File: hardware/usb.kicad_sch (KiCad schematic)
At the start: 51 parts, among them J1 USB_C_Receptacle_USB2.0_14P, J27 USB_C_Receptacle_USB2.0_14P, J28 USB_C_Receptacle_USB2.0_14P, Q1 BSC098N10NS5, Q2 BSC098N10NS5, SW1 SW_DIP_x03, SW2 SW_DIP_x03, U2 CH224K, U20 LM5050-1, U21 LM5050-1, U22 CH224K

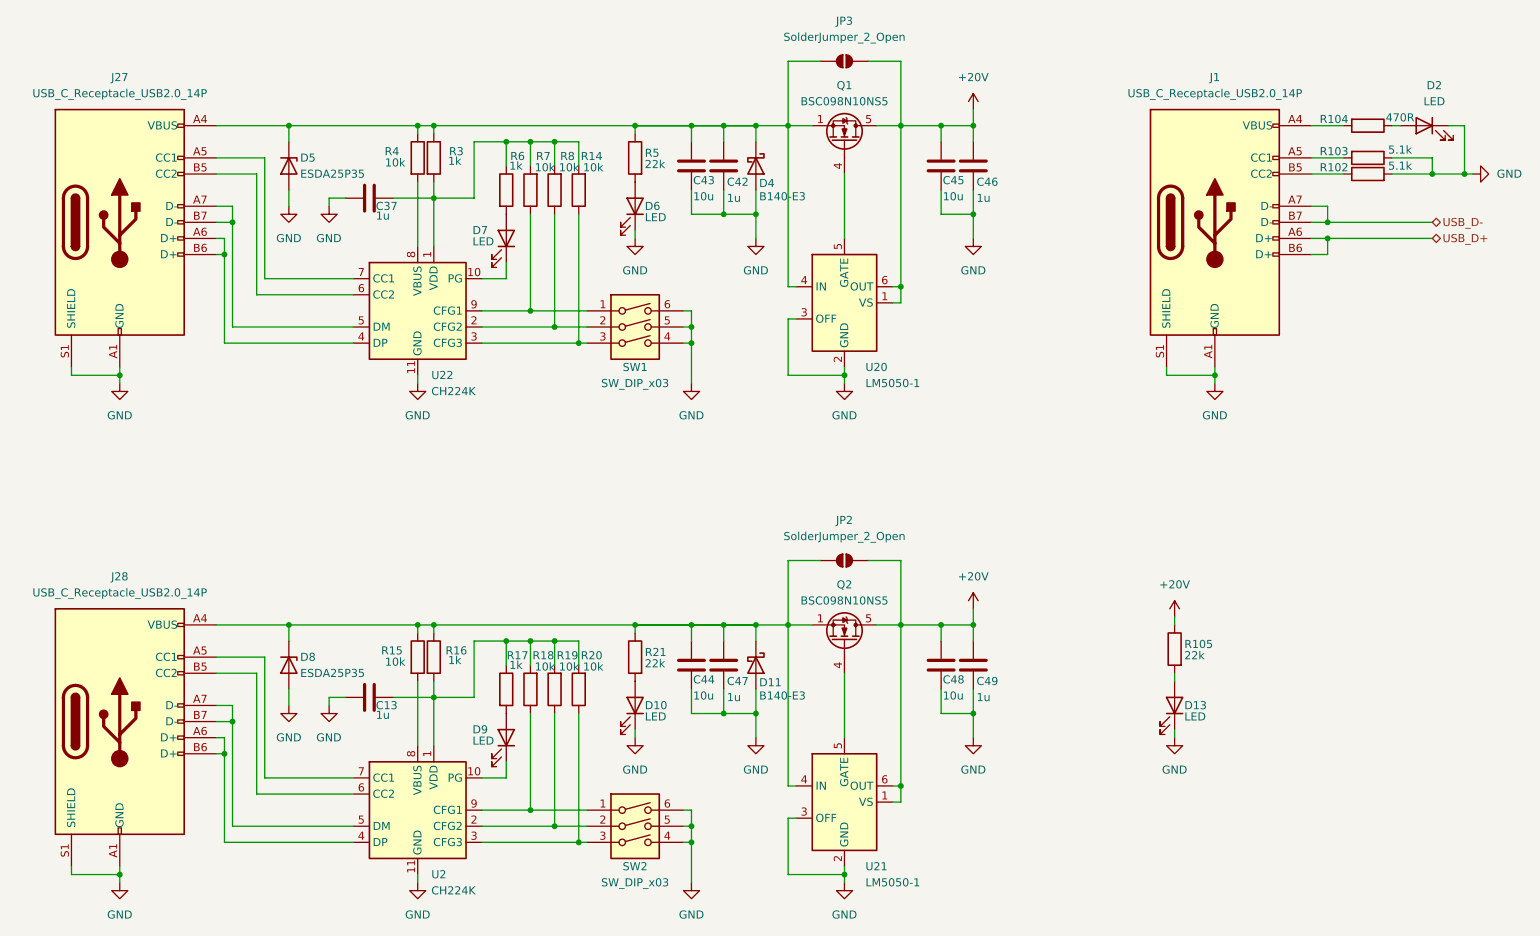
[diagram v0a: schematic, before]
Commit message: complete schematic wiring
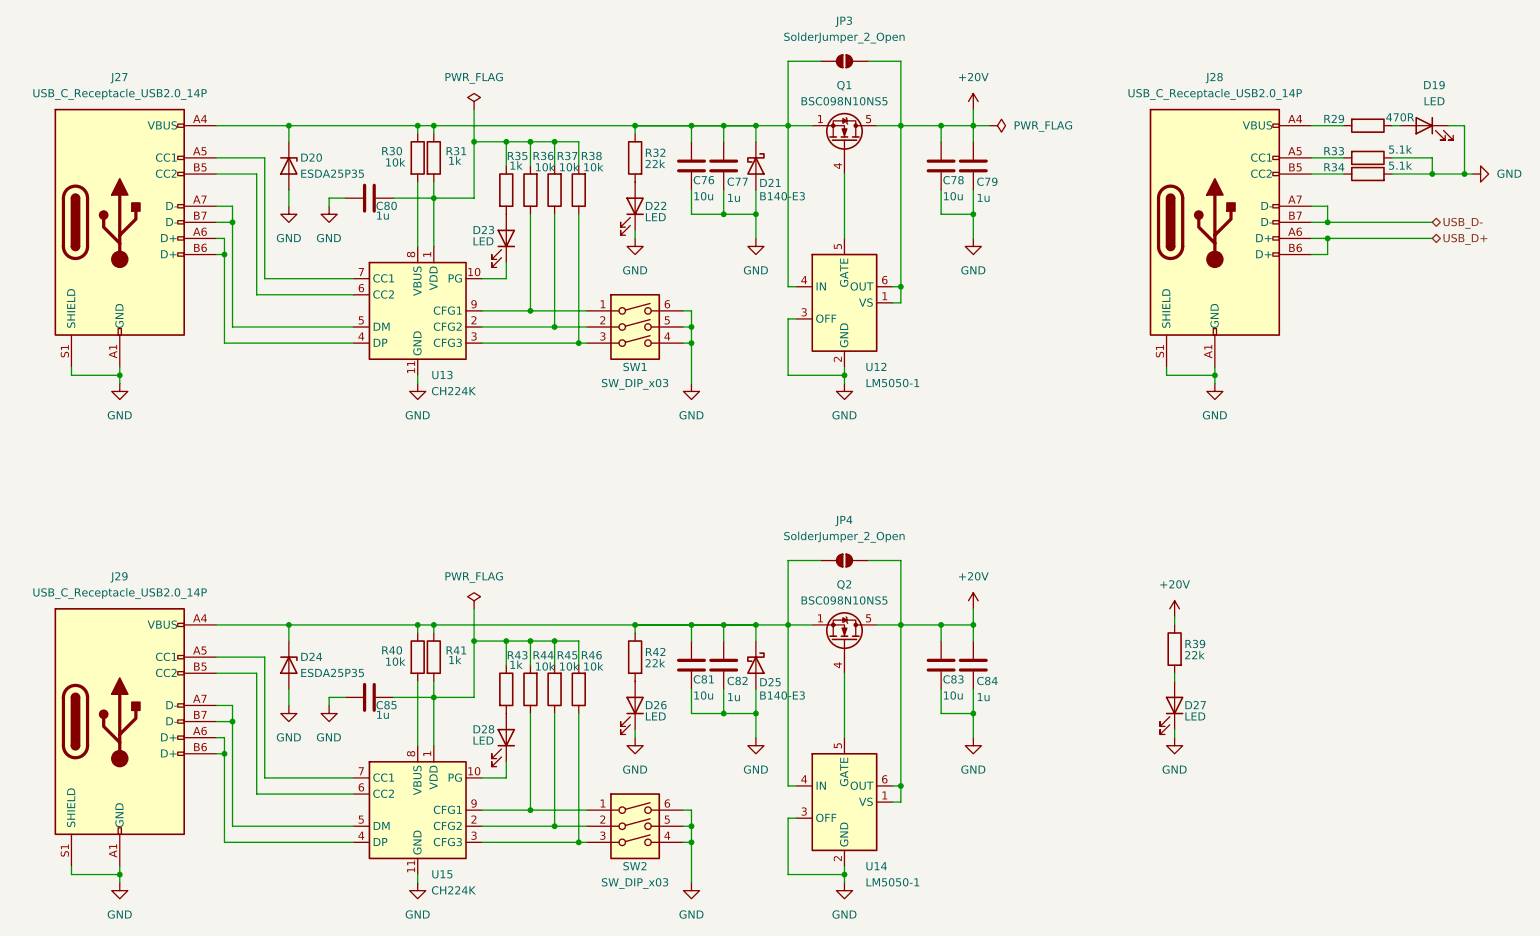
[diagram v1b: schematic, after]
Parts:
- renumbered C43 to C76, C42 to C77, C45 to C78, C46 to C79, C37 to C80, C44 to C81, C47 to C82, C48 to C83, C49 to C84, C13 to C85, D2 to D19, D5 to D20, D4 to D21, D6 to D22, D7 to D23, D8 to D24, D11 to D25, D10 to D26, D13 to D27, D9 to D28, J1 to J28, J28 to J29, JP2 to JP4, R104 to R29, R4 to R30, R3 to R31, R5 to R32, R103 to R33, R102 to R34, R6 to R35, R7 to R36, R8 to R37, R14 to R38, R105 to R39, R15 to R40, R16 to R41, R21 to R42, R17 to R43, R18 to R44, R19 to R45, R20 to R46, U20 to U12, U22 to U13, U21 to U14, U2 to U15

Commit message: update power system + add LCSC part numbers
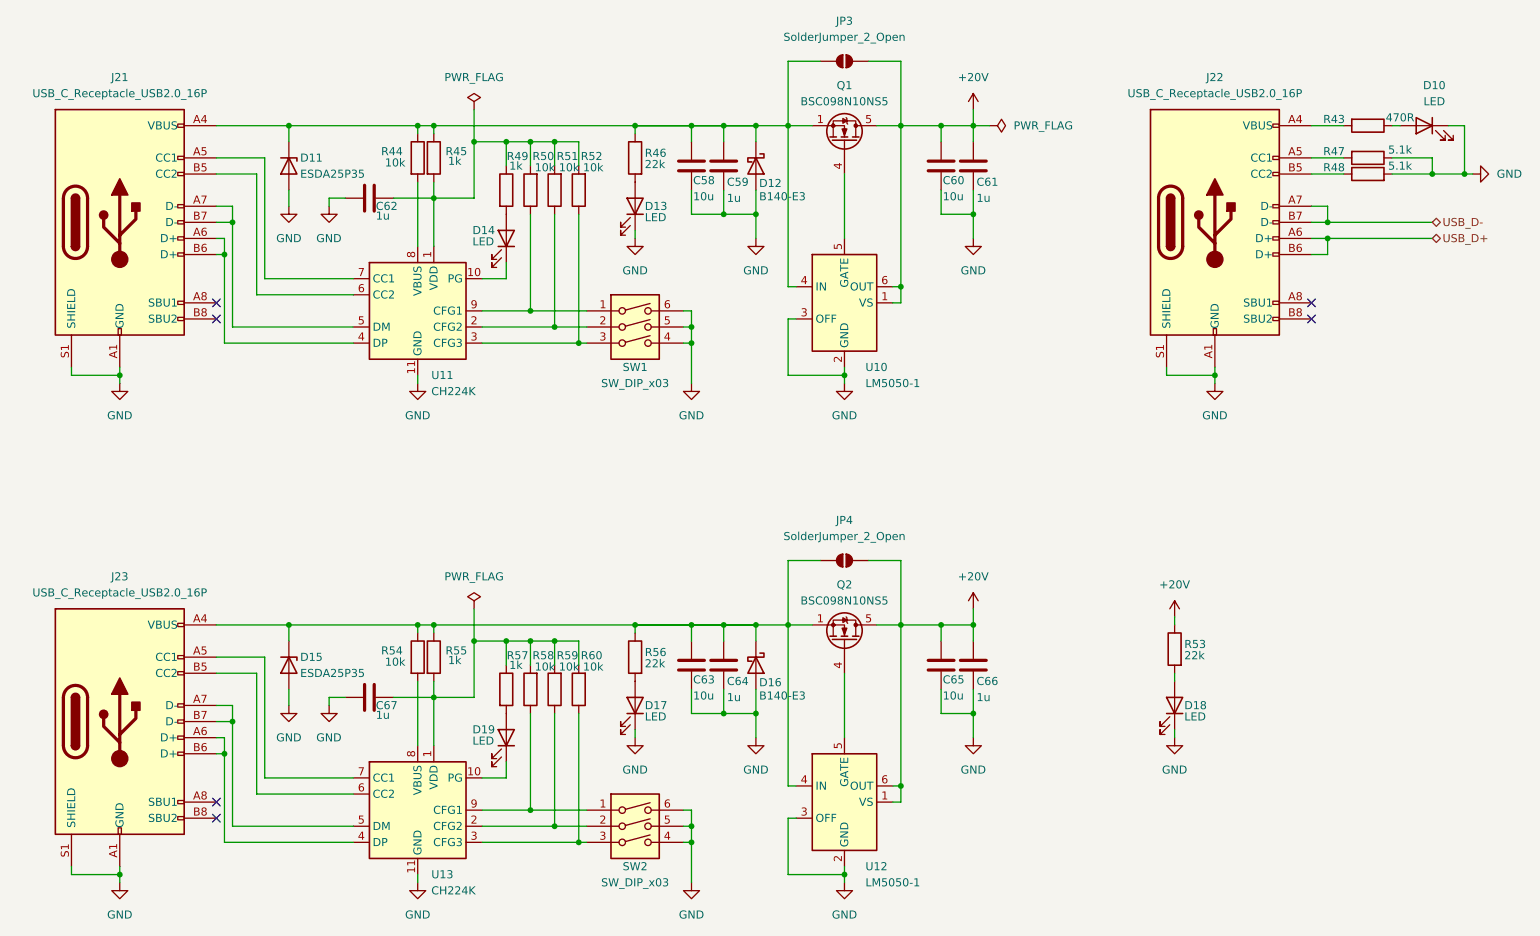
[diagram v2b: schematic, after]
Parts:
- removed J27, J28, J29: USB_C_Receptacle_USB2.0_14P, symbol Connector:USB_C_Receptacle_USB2.0_14P
- added J21, J22, J23: USB_C_Receptacle_USB2.0_16P, Connector_USB:USB_C_Receptacle_GCT_USB4105-xx-A_16P_TopMnt_Horizontal, symbol Connector:USB_C_Receptacle_USB2.0_16P
- C58: renamed from C76; footprint (none) -> Capacitor_SMD:C_1206_3216Metric; LCSC (none) -> C13585
- C59: renamed from C77; footprint (none) -> Capacitor_SMD:C_0805_2012Metric; LCSC (none) -> C28323
- C60: renamed from C78; footprint (none) -> Capacitor_SMD:C_1206_3216Metric; LCSC (none) -> C13585
- C61: renamed from C79; footprint (none) -> Capacitor_SMD:C_0805_2012Metric; LCSC (none) -> C28323
- C62: renamed from C80; footprint (none) -> Capacitor_SMD:C_0805_2012Metric; LCSC (none) -> C28323
- C63: renamed from C81; footprint (none) -> Capacitor_SMD:C_1206_3216Metric; LCSC (none) -> C13585
- C64: renamed from C82; footprint (none) -> Capacitor_SMD:C_0805_2012Metric; LCSC (none) -> C28323
- C65: renamed from C83; footprint (none) -> Capacitor_SMD:C_1206_3216Metric; LCSC (none) -> C13585
- C66: renamed from C84; footprint (none) -> Capacitor_SMD:C_0805_2012Metric; LCSC (none) -> C28323
- C67: renamed from C85; footprint (none) -> Capacitor_SMD:C_0805_2012Metric; LCSC (none) -> C28323
- D10: renamed from D19; footprint (none) -> LED_SMD:LED_0805_2012Metric; LCSC (none) -> C2297
- D11: renamed from D20; footprint (none) -> digital:D_1610_4027Metric; LCSC (none) -> C1974707
- D12: renamed from D21; LCSC (none) -> C2981056
- D13: renamed from D22; footprint (none) -> LED_SMD:LED_0805_2012Metric; LCSC (none) -> C2297
- D14: renamed from D23; footprint (none) -> LED_SMD:LED_0805_2012Metric; LCSC (none) -> C2297
- D15: renamed from D24; footprint (none) -> digital:D_1610_4027Metric; LCSC (none) -> C1974707
- D16: renamed from D25; LCSC (none) -> C2981056
- D17: renamed from D26; footprint (none) -> LED_SMD:LED_0805_2012Metric; LCSC (none) -> C2297
- D18: renamed from D27; footprint (none) -> LED_SMD:LED_0805_2012Metric; LCSC (none) -> C2297
- D19: renamed from D28; footprint (none) -> LED_SMD:LED_0805_2012Metric; LCSC (none) -> C2297
- JP3, JP4: footprint (none) -> Jumper:SolderJumper-2_P1.3mm_Open_RoundedPad1.0x1.5mm
- Q1, Q2: LCSC (none) -> C534398
- R43: renamed from R29; footprint (none) -> Resistor_SMD:R_0402_1005Metric; LCSC (none) -> C25117
- R44: renamed from R30; footprint (none) -> Resistor_SMD:R_0402_1005Metric; LCSC (none) -> C25744
- R45: renamed from R31; footprint (none) -> Resistor_SMD:R_0402_1005Metric; LCSC (none) -> C11702
- R46: renamed from R32; footprint (none) -> Resistor_SMD:R_0402_1005Metric; LCSC (none) -> C25768
- R47: renamed from R33; footprint (none) -> Resistor_SMD:R_0402_1005Metric; LCSC (none) -> C25905
- R48: renamed from R34; footprint (none) -> Resistor_SMD:R_0402_1005Metric; LCSC (none) -> C25905
- R49: renamed from R35; footprint (none) -> Resistor_SMD:R_0402_1005Metric; LCSC (none) -> C11702
- R50: renamed from R36; footprint (none) -> Resistor_SMD:R_0402_1005Metric; LCSC (none) -> C25744
- R51: renamed from R37; footprint (none) -> Resistor_SMD:R_0402_1005Metric; LCSC (none) -> C25744
- R52: renamed from R38; footprint (none) -> Resistor_SMD:R_0402_1005Metric; LCSC (none) -> C25744
- R53: renamed from R39; footprint (none) -> Resistor_SMD:R_0402_1005Metric; LCSC (none) -> C25768
- R54: renamed from R40; footprint (none) -> Resistor_SMD:R_0402_1005Metric; LCSC (none) -> C25744
- R55: renamed from R41; footprint (none) -> Resistor_SMD:R_0402_1005Metric; LCSC (none) -> C11702
- R56: renamed from R42; footprint (none) -> Resistor_SMD:R_0402_1005Metric; LCSC (none) -> C25768
- R57: renamed from R43; footprint (none) -> Resistor_SMD:R_0402_1005Metric; LCSC (none) -> C11702
- R58: renamed from R44; footprint (none) -> Resistor_SMD:R_0402_1005Metric; LCSC (none) -> C25744
- R59: renamed from R45; footprint (none) -> Resistor_SMD:R_0402_1005Metric; LCSC (none) -> C25744
- R60: renamed from R46; footprint (none) -> Resistor_SMD:R_0402_1005Metric; LCSC (none) -> C25744
- SW1, SW2: footprint (none) -> Button_Switch_SMD:SW_DIP_SPSTx03_Slide_6.7x9.18mm_W8.61mm_P2.54mm_LowProfile; LCSC (none) -> C129079
- U10: renamed from U12; LCSC (none) -> C129323
- U11: renamed from U13; LCSC (none) -> C970725
- U12: renamed from U14; LCSC (none) -> C129323
- U13: renamed from U15; LCSC (none) -> C970725
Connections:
- net GND: now also J21.A1 (GND), J21.A12 (GND), J21.B1 (GND), J21.B12 (GND), J21.S1 (SHIELD), J22.A1 (GND), J22.A12 (GND), J22.B1 (GND), J22.B12 (GND), J22.S1 (SHIELD), J23.A1 (GND), J23.A12 (GND), J23.B1 (GND), J23.B12 (GND), J23.S1 (SHIELD)
- net USB_D+: now also J22.A6 (D+), J22.B6 (D+)
- net USB_D-: now also J22.A7 (D-), J22.B7 (D-)
- net at C63.1, C64.1, D15.1 (K)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: now also J23.A4 (VBUS), J23.A9 (VBUS), J23.B4 (VBUS), J23.B9 (VBUS)
- net at U13.7 (CC1): now also J23.A5 (CC1)
- net at U13.4 (DP): now also J23.A6 (D+), J23.B6 (D+)
- net at U13.5 (DM): now also J23.A7 (D-), J23.B7 (D-)
- net at U13.6 (CC2): now also J23.B5 (CC2)
- net at C58.1, C59.1, D11.1 (K)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: now also J21.A4 (VBUS), J21.A9 (VBUS), J21.B4 (VBUS), J21.B9 (VBUS)
- net at U11.4 (DP): now also J21.A6 (D+), J21.B6 (D+)
- net at U11.5 (DM): now also J21.A7 (D-), J21.B7 (D-)
- net at U11.6 (CC2): now also J21.B5 (CC2)
- net at U11.7 (CC1): now also J21.A5 (CC1)
- net at R48.1: now also J22.B5 (CC2)
- net at R43.2: now also J22.A4 (VBUS), J22.A9 (VBUS), J22.B4 (VBUS), J22.B9 (VBUS)
- net at R47.2: now also J22.A5 (CC1)
- no-connect marks 0 -> 6

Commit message: apply manufacturing BOM
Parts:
- renumbered C58 to C62, C59 to C63, C60 to C64, C61 to C65, C62 to C66, C63 to C67, C64 to C68, C65 to C69, C66 to C70, C67 to C71, J21 to J20, J22 to J21, J23 to J22, R43 to R51, R44 to R52, R45 to R53, R46 to R54, R47 to R55, R48 to R56, R49 to R57, R50 to R58, R51 to R59, R52 to R60, R53 to R61, R54 to R62, R55 to R63, R56 to R64, R57 to R65, R58 to R66, R59 to R67, R60 to R68

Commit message: route
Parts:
- removed C62, C64, C69: 10u, Capacitor_SMD:C_1206_3216Metric, symbol Device:C
- removed C63, C65, C66, C70: 1u, Capacitor_SMD:C_0805_2012Metric, symbol Device:C
- removed D11: ESDA25P35, digital:D_1610_4027Metric, symbol Device:D_Zener
- removed D12, D16: B140-E3, Diode_SMD:D_SMA, symbol Diode:B140-E3
- removed D13, D14, D18: LED, LED_SMD:LED_0805_2012Metric, symbol Device:LED
- removed J20: USB_C_Receptacle_USB2.0_16P, Connector_USB:USB_C_Receptacle_GCT_USB4105-xx-A_16P_TopMnt_Horizontal, symbol Connector:USB_C_Receptacle_USB2.0_16P
- removed JP3, JP4: SolderJumper_2_Open, Jumper:SolderJumper-2_P1.3mm_Open_RoundedPad1.0x1.5mm, symbol Jumper:SolderJumper_2_Open
- removed Q1, Q2: BSC098N10NS5, Package_TO_SOT_SMD:TDSON-8-1, symbol Transistor_FET:BSC098N10NS5
- removed R52, R58, R59, R60: 10k, Resistor_SMD:R_0402_1005Metric, symbol Device:R
- removed R53, R57: 1k, Resistor_SMD:R_0402_1005Metric, symbol Device:R
- removed R54, R61: 22k, Resistor_SMD:R_0402_1005Metric, symbol Device:R
- removed SW1: SW_DIP_x03, Button_Switch_SMD:SW_DIP_SPSTx03_Slide_6.7x9.18mm_W8.61mm_P2.54mm_LowProfile, symbol Switch:SW_DIP_x03
- removed U10, U12: LM5050-1, Package_TO_SOT_SMD:TSOT-23-6, symbol Power_Management:LM5050-1
- removed U11: CH224K, Package_SO:SSOP-10-1EP_3.9x4.9mm_P1mm_EP2.1x3.3mm, symbol Interface_USB:CH224K
- renumbered C67 to C65, C68 to C66, C71 to C67, D15 to D10, D17 to D11, D19 to D12, D10 to D13, J22 to J19, J21 to J20, R62 to R51, R63 to R52, R64 to R53, R65 to R54, R66 to R55, R67 to R56, R68 to R57, R51 to R58, R55 to R59, R56 to R60, SW2 to SW1, U13 to U10
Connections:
- net +20V: now also C65.1, C66.1, D10.1 (K), J19.A4 (VBUS), J19.A9 (VBUS), J19.B4 (VBUS), J19.B9 (VBUS), R51.1, R52.1, R53.1
- no-connect marks 6 -> 4
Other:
- moved on the sheet: C65, C66, C67, D10, D11, D12, D13, J19, J20, R51, R52, R53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

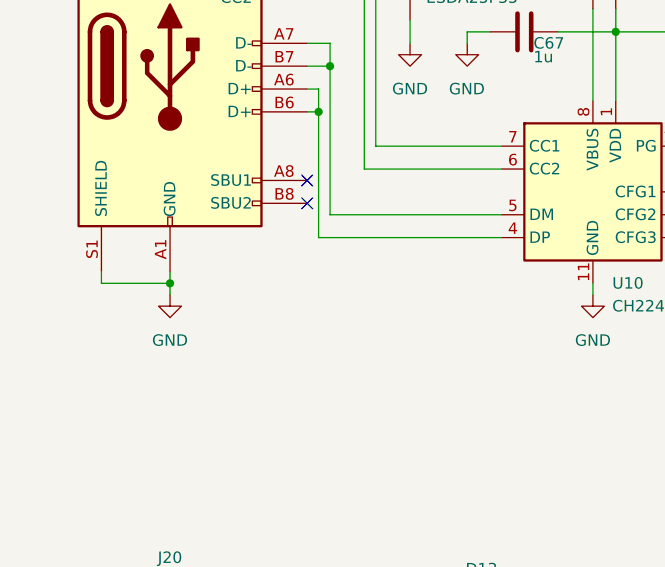
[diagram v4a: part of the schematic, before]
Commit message: route all signal
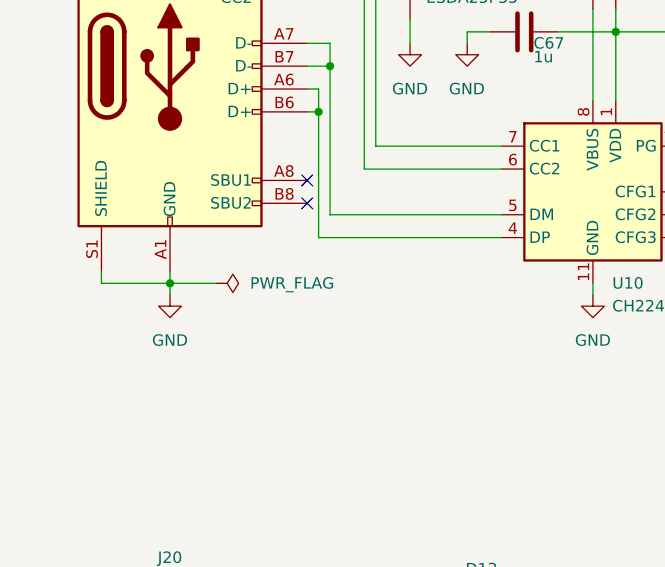
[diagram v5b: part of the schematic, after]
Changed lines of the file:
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@@
+	(wire
+		(pts
+			(xy 54.61 83.82) (xy 59.69 83.82)
+		)
+		(stroke
+			(width 0)
+			(type default)
+		)
+	)
 	(wire
 		(pts
@@
 					(unit 1)
 				)
+			)
+		)
+	)
+	(symbol
+		(lib_id "power:PWR_FLAG")
+		(at 59.69 83.82 270)
+		(unit 1)
+		(exclude_from_sim no)
+		(in_bom yes)
+		(on_board yes)
+		(dnp no)
+		(fields_autoplaced yes)
+		(property "Reference" "#FLG014"
+			(at 61.595 83.82 0)
+			(effects
+				(font
+					(size 1.27 1.27)
+				)
+				(hide yes)
+			)
+		)
+		(property "Value" "PWR_FLAG"
+			(at 63.5 83.8199 90)
+			(effects
+				(font
+					(size 1.27 1.27)
+				)
+				(justify left)
+			)
+		)
+		(property "Footprint" ""
+			(at 59.69 83.82 0)
+			(effects
+				(font
+					(size 1.27 1.27)
+				)
+				(hide yes)
+			)
+		)
+		(property "Datasheet" "~"
+			(at 59.69 83.82 0)
+			(effects
+				(font
+					(size 1.27 1.27)
+				)
+				(hide yes)
+			)
+		)
+		(property "Description" "Special symbol for telling ERC where power comes from"
+			(at 59.69 83.82 0)
+			(effects
+				(font
+					(size 1.27 1.27)
+				)
+				(hide yes)
+			)
+		)
+		(pin "1"
+		)
+		(instances
+			(project "digital"
+				(path "/4c5c7ce5-09d6-4a32-b2a0-f32b0c47f27d/6e83fa56-1de6-4a8a-b621-b1c47cfad8d5"
+					(reference "#FLG014")
+					(unit 1)
+				)
